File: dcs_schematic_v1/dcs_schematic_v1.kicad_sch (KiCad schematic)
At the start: 41 parts, among them J1 to_encoder, M1 Motor_DC, Q1 IRLZ44N, Q2 IRLZ44N, Q3 IRLZ44N, Q4 IRLZ44N, U1 LM331N, U2A_differential TL084, U2B_proportional TL084, U3A_integral TL084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

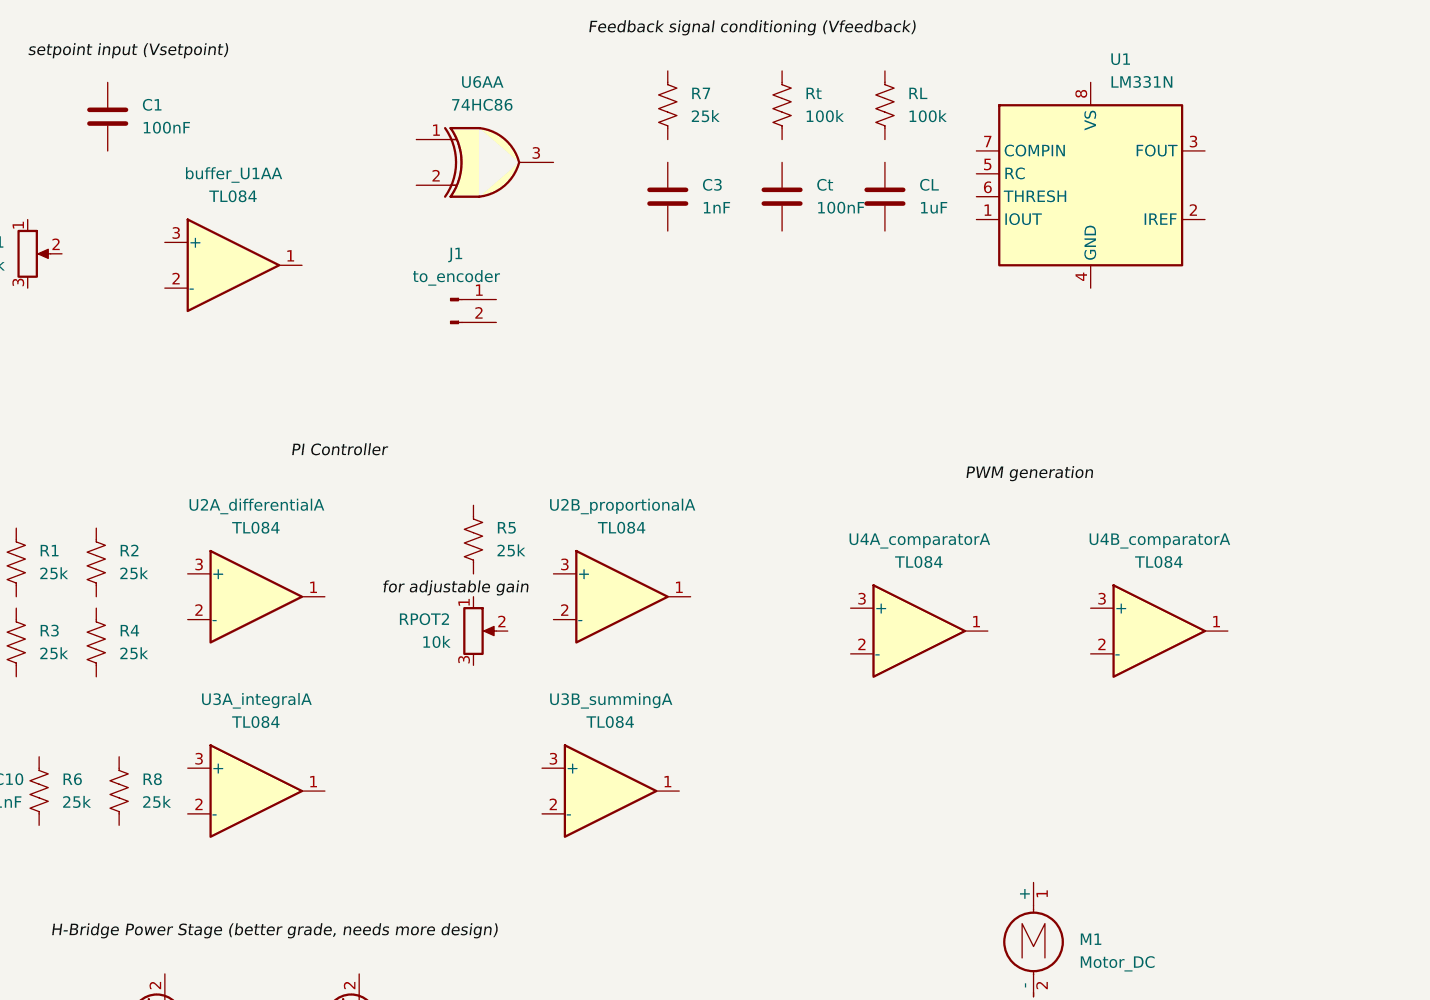
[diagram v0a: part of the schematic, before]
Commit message: changed ti084 to opa2197xD in schematic. swapped datasheets
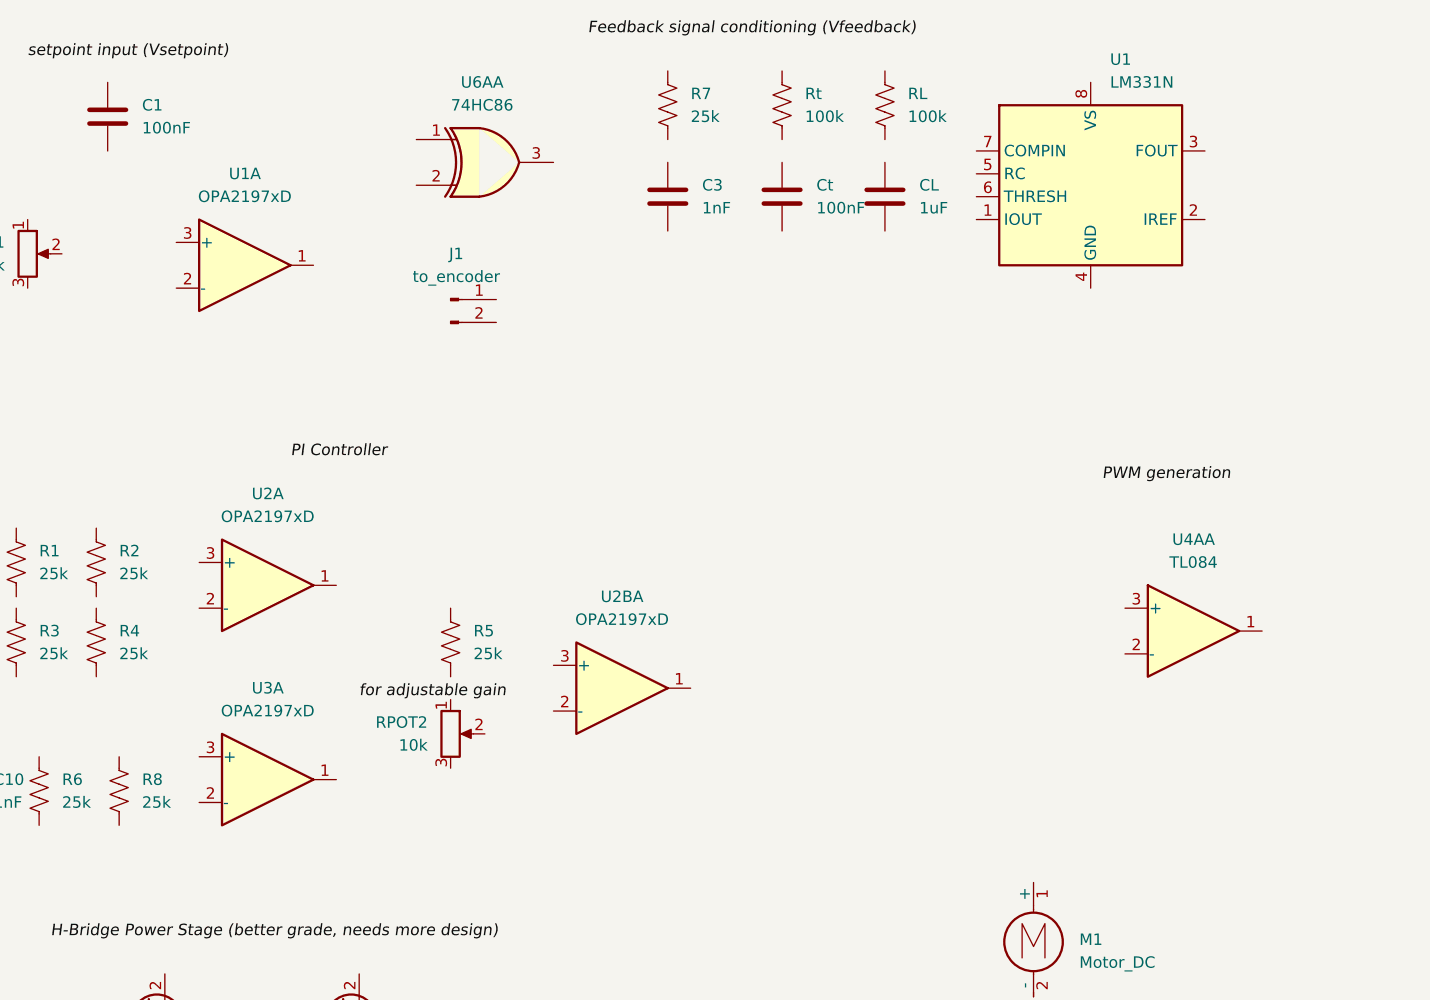
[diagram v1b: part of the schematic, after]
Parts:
- removed U2A_differential, U2B_proportional, U3A_integral, U3B_summing, U4B_comparator, buffer_U1A: TL084, symbol Amplifier_Operational:TL084
- added U1, U2, U2B, U3: OPA2197xD, Package_SO:SOIC-8_3.9x4.9mm_P1.27mm, symbol Amplifier_Operational:OPA2197xD
- renumbered U4A_comparator to U4A
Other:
- moved on the sheet: R5, RPOT2, U4AA

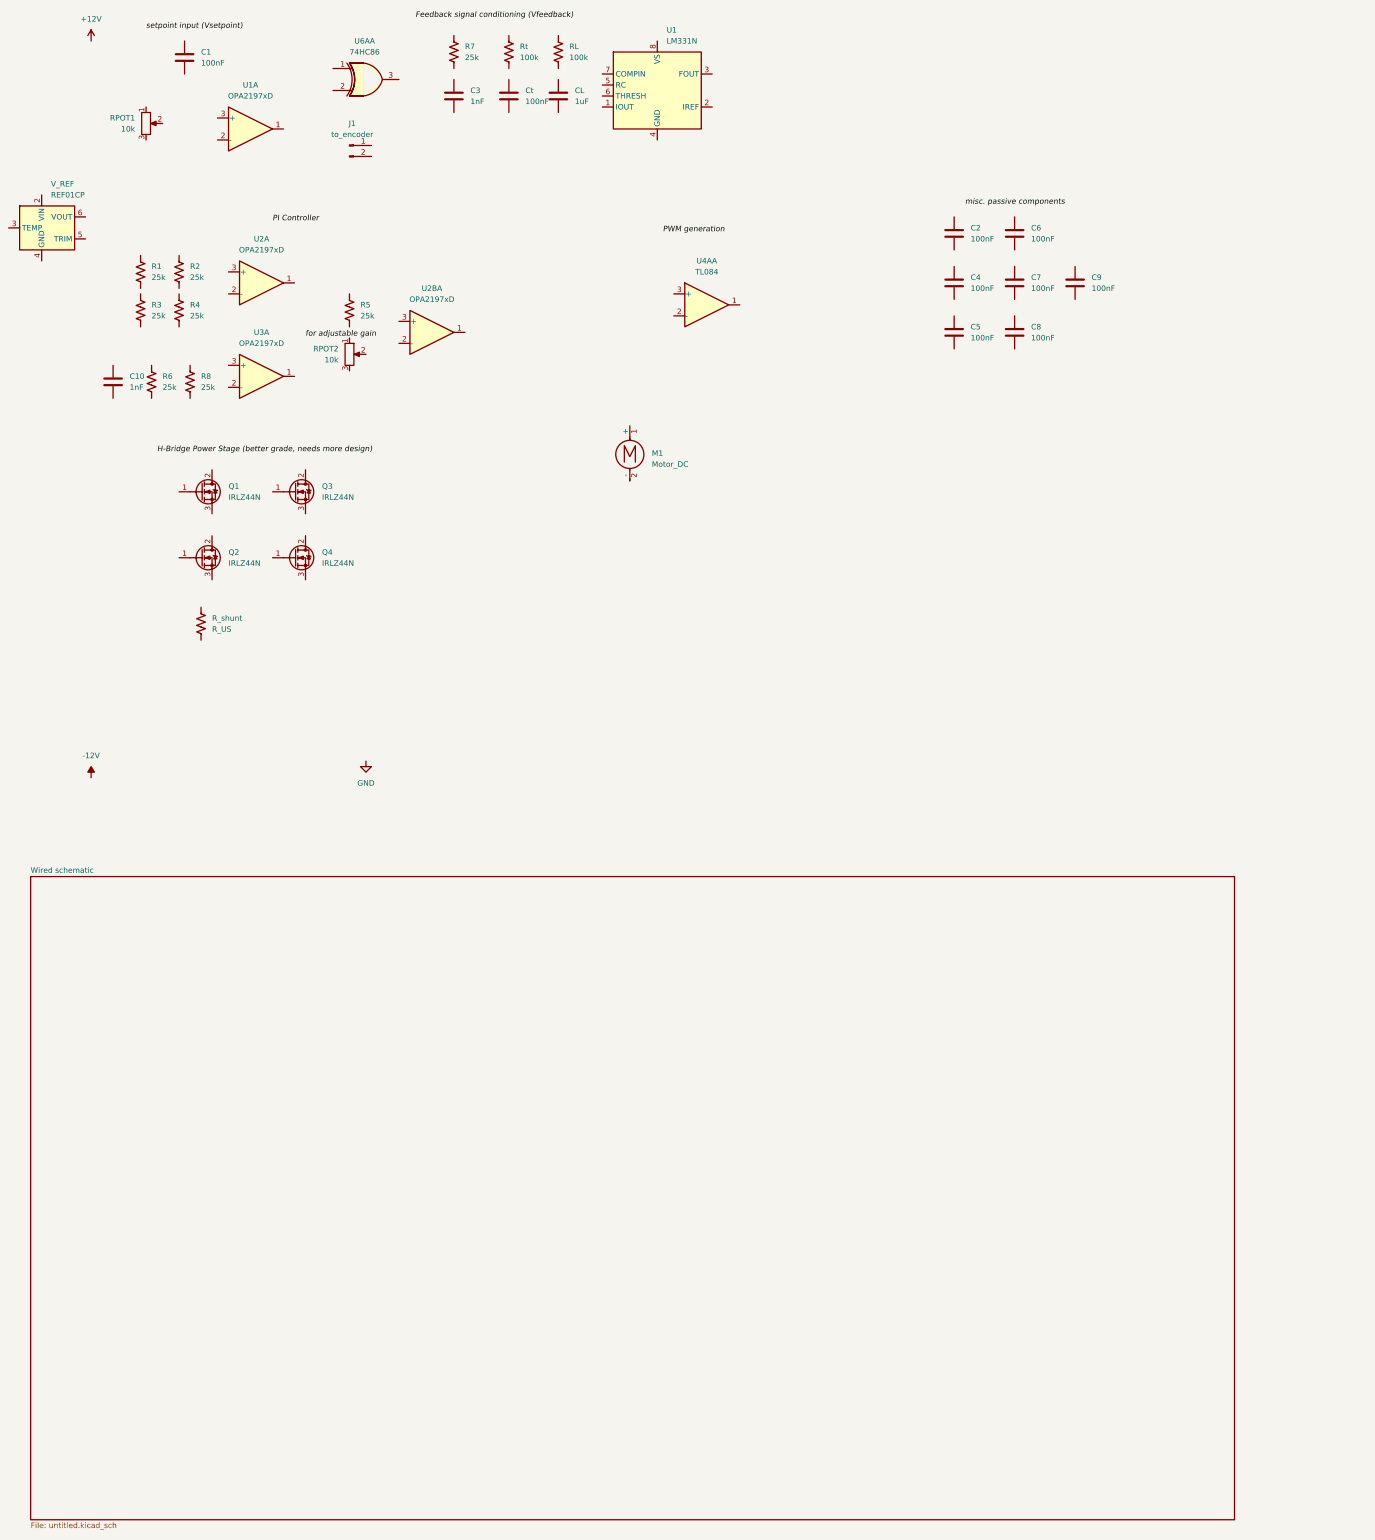
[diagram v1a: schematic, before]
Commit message: first version of wiring schematic 85% done
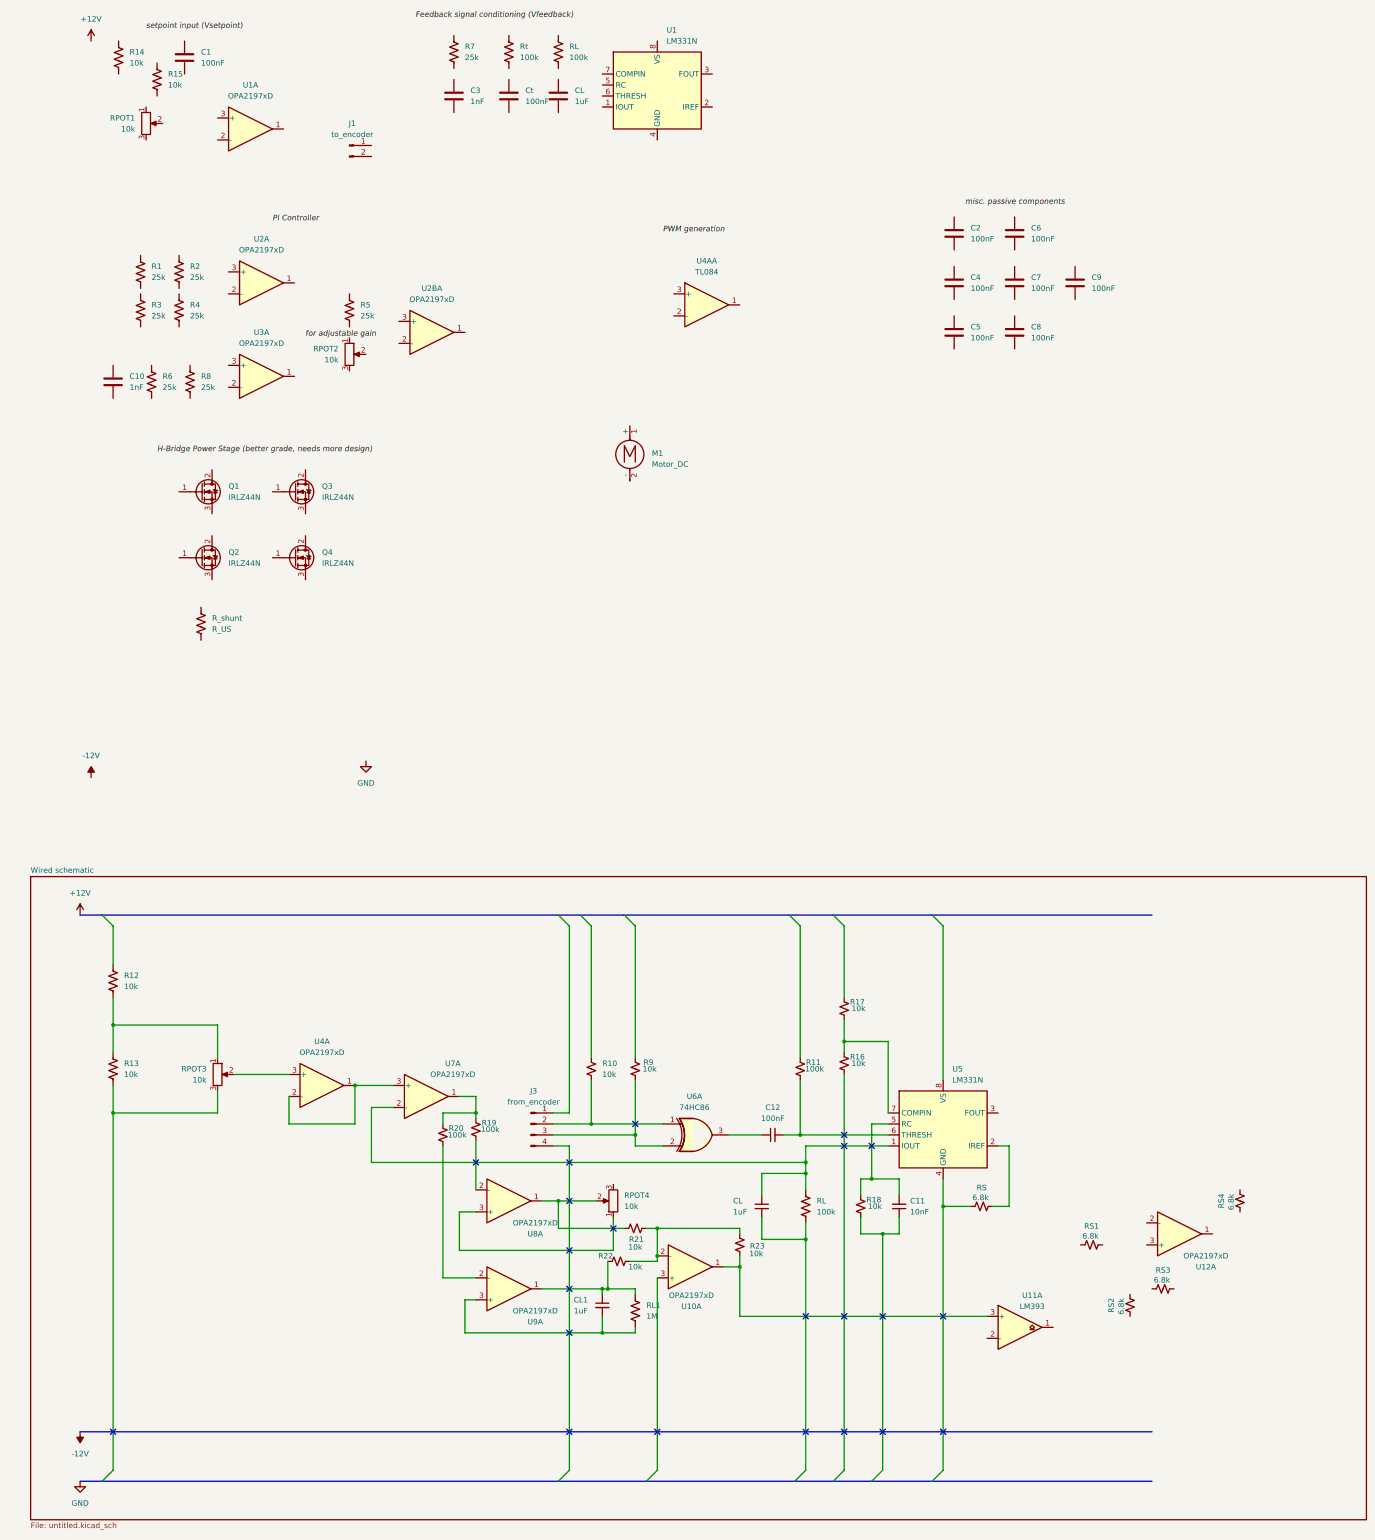
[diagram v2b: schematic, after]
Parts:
- removed U6A: 74HC86, symbol 74xx:74HC86
- removed V_REF: REF01CP, Package_DIP:DIP-8_W7.62mm, symbol Reference_Voltage:REF01CP
- added C11: 10nF, symbol Device:C_Small
- added C12: 100nF, symbol Device:C_Small
- added CL, CL1: 1uF, symbol Device:C_Small
- added J3: from_encoder, symbol Connector:Conn_01x04_Pin
- added R10, R16, R17, R18, R21, R22, R23, R9: 10k, symbol Device:R_Small_US
- added R11, R19, R20: 100k, symbol Device:R_Small_US
- added R12, R13, R14, R15: 10k, symbol Device:R_US
- added RL: 100k, symbol Device:R_US
- added RL1: 1M, symbol Device:R_US
- added RPOT3, RPOT4: 10k, symbol Device:R_Potentiometer
- added RS, RS1, RS2, RS3, RS4: 6.8k, symbol Device:R_Small_US
- added U10, U12, U4, U7, U8, U9: OPA2197xD, Package_SO:SOIC-8_3.9x4.9mm_P1.27mm, symbol Amplifier_Operational:OPA2197xD
- added U11: LM393, symbol Comparator:LM393
- added U5: LM331N, Package_DIP:DIP-8_W7.62mm, symbol Analog:LM331N
- added U6: 74HC86, symbol 74xx:74HC86
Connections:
- new net: C11.1, R18.1
- new net: C11.2, R18.2, U5.5 (RC)
- new net: R21.1, R22.1, R23.2, U10.2 (-)
- new net: CL1.1, R22.2, RL1.1, U9.1
- new net: R21.2, RPOT4.2, U8.1
- new net: R19.1, U8.2 (-)
- new net: RPOT4.1, U8.3 (+)
- new net: CL.1, RL.1, U5.1 (IOUT), U7.2 (-)
- new net: CL.2, RL.2
- new net: C12.1, U6.3
- new net: C12.2, R11.1, U5.6 (THRESH)
- new net: RS.1, U5.2 (IREF)
- new net: RS.2, U5.4 (GND)
- new net: R16.2, R17.1, U5.7 (COMPIN)
- new net: R19.2, R20.2, U7.1
- new net: R12.2, R13.1, RPOT3.1
- new net: R13.2, RPOT3.3
- new net: J3.2 (Pin_2), R10.1, U6.1
- new net: J3.3 (Pin_3), R9.1, U6.2
- new net: CL1.2, RL1.2, U9.3 (+)
- new net: R23.1, U10.1, U11.3 (+)
- new net: U4.1, U4.2 (-), U7.3 (+)
- new net: RPOT3.2, U4.3 (+)
- new net: R20.1, U9.2 (-)
- no-connect marks 0 -> 22

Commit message: finished v1 of wired circuit
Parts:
- removed RS1, RS2, RS3, RS4: 6.8k, symbol Device:R_Small_US
- removed U11: LM393, symbol Comparator:LM393
- added C_freq: 10nF, symbol Device:C_Small
- added D1: 1N5819, Diode_THT:D_DO-41_SOD81_P10.16mm_Horizontal, symbol Diode:1N5819
- added M2: Motor_DC, symbol Motor:Motor_DC
- added Q5: IRLZ44N, Package_TO_SOT_THT:TO-220-3_Vertical, symbol Transistor_FET:IRLZ44N
- added R19, R24, R_freq, R_gs: 10k, symbol Device:R_Small_US
- added U11: OPA2197xD, Package_SO:SOIC-8_3.9x4.9mm_P1.27mm, symbol Amplifier_Operational:OPA2197xD
- added U13: LM311, symbol Comparator:LM311
- renumbered U12 to U4
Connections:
- net at U4.1: now also C_freq.1, U11.3 (+), U13.3 (-)
- net at U4.2 (-): now also C_freq.2, R_freq.1
- net at U4.3 (+): now also Q5.3 (S), R_gs.1
- net at R23.1, U10.1: now also U13.2 (+)
- new net: Q5.1 (G), R_gs.2, U13.7
- new net: D1.2 (A), M2.2 (-), Q5.2 (D)
- new net: R24.1, R_freq.2, U11.1
- new net: R19.2, R24.2, U11.2 (-)
- new net: D1.1 (K), M2.1 (+)
- no-connect marks 22 -> 29
